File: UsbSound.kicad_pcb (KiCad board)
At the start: 4 copper layers, 121.6 x 79.8 mm, 85 parts, among them J1 SWD, J2 USB_B, J3 XLR_L, J4 XLR_R, SW1 BOOT_SELECT, U1 MP2359-LF-Z, U2 USBLC6-2SC6, U3 NE5534, U4 PCM1795DB, U5 STM32F405RGT6, U6 NE5534, U7 NE5534, U8 NE5534, Y1 16MHz, Y2 36.864MHz

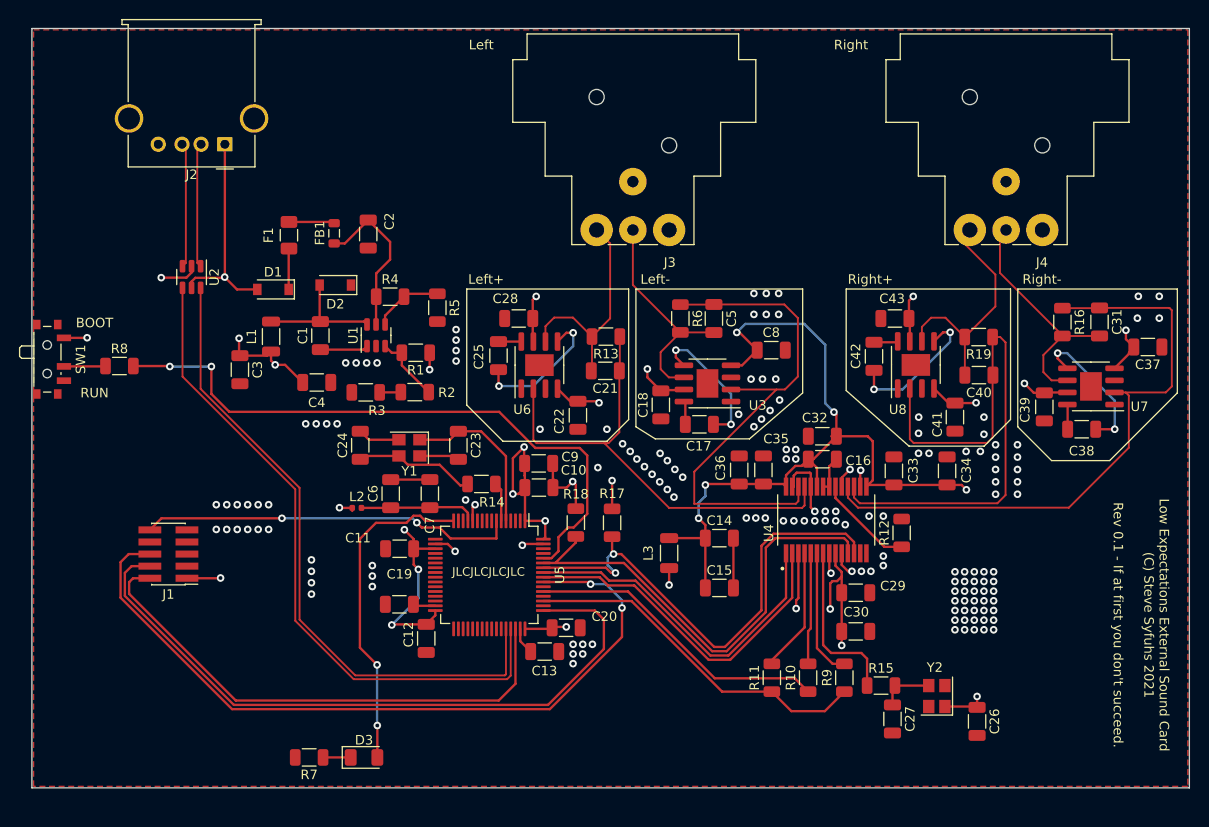
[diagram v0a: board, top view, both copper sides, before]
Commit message: Added -5v rail because I'm an idiot and forgot it
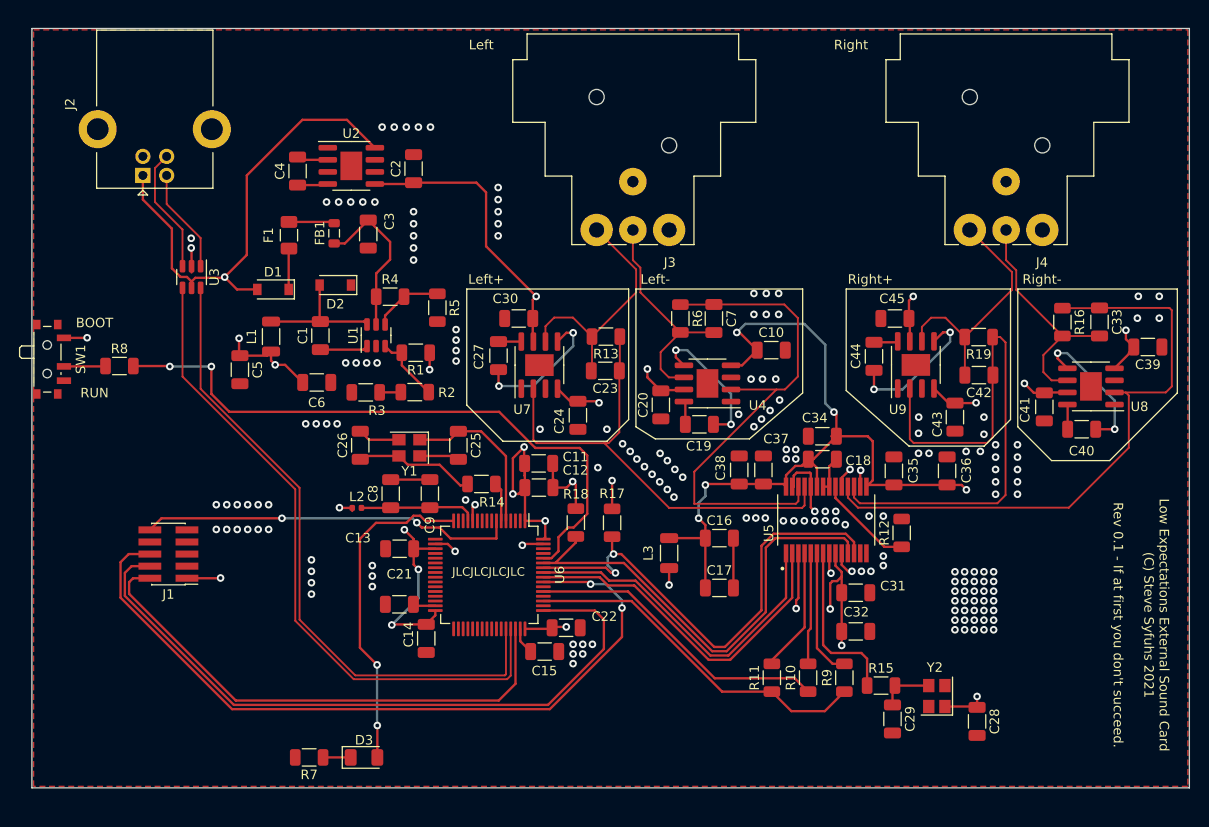
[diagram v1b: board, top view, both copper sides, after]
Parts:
- added C2: 10u, Capacitor_SMD:C_1206_3216Metric, F.Cu at (116.3, 56.2)
- added C4: 10u, Capacitor_SMD:C_1206_3216Metric, F.Cu at (104.1, 56.4)
- added U2: ICL7660, Package_SO:SOIC-8-1EP_3.9x4.9mm_P1.27mm_EP2.29x3mm, F.Cu at (109.8, 55.9)
- J2: footprint Connector_USB:USB_A_Molex_67643_Horizontal -> Connector_USB:USB_B_Lumberg_2411_02_Horizontal
- moved J2 9.22 mm to (87.9, 56.9), turned to 90 degrees
- renumbered C8 to C10, C9 to C11, C10 to C12, C11 to C13, C12 to C14, C13 to C15, C14 to C16, C15 to C17, C16 to C18, C17 to C19, C18 to C20, C19 to C21, C20 to C22, C21 to C23, C22 to C24, C23 to C25, C24 to C26, C25 to C27, C26 to C28, C27 to C29, C2 to C3, C28 to C30, C29 to C31, C30 to C32, C31 to C33, C32 to C34, C33 to C35, C34 to C36, C35 to C37, C36 to C38, C37 to C39, C38 to C40, C39 to C41, C40 to C42, C41 to C43, C42 to C44, C43 to C45, C3 to C5, C4 to C6, C5 to C7, C6 to C8, C7 to C9, U2 to U3, U3 to U4, U4 to U5, U5 to U6, U6 to U7, U7 to U8, U8 to U9
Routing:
- net +5V: track 88.0 -> 116.5 mm
- net -5VA: track 97.9 -> 123.2 mm
- net Net-(C4-Pad2): track 0.00 -> 3.30 mm
- net Net-(C4-Pad1): track 0.00 -> 3.22 mm
- net XLR_R+: track 23.9 -> 26.4 mm
- net XLR_L+: track 23.8 -> 26.1 mm
- net USB_CONN_D-: track 12.6 -> 11.0 mm
- net GND: track 54.9 -> 53.4 mm, vias 157 -> 178
- net XLR_R-: track 23.8 -> 25.0 mm
- net USB_CONN_D+: track 12.6 -> 13.3 mm

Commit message: Op Amps are better paired for line matching
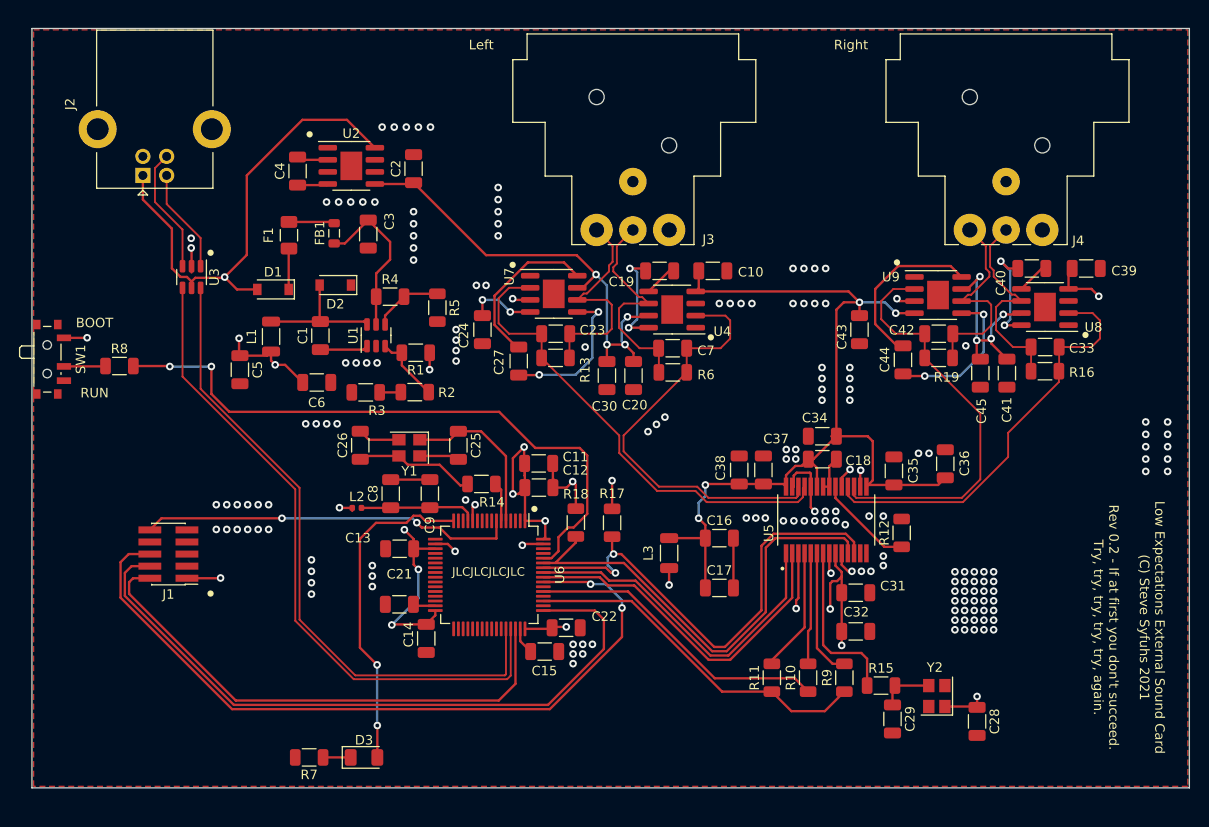
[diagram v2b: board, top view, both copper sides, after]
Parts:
- moved C40 17.7 mm to (181.3, 66.7)
- moved C19 16.7 mm to (142.2, 66.9)
- moved C43 13.6 mm to (163.2, 73.1)
- moved C24 13.5 mm to (123.6, 73.1)
- moved C30 11.0 mm to (136.7, 77.9), turned to 90 degrees
- moved C45 10.7 mm to (175.9, 77.7), turned to 90 degrees
- moved C39 10.5 mm to (187.0, 66.7)
- moved C10 10.4 mm to (147.8, 66.9)
- moved U8 9.64 mm to (182.7, 70.7)
- moved U4 8.61 mm to (143.5, 71.0)
- moved U9 7.70 mm to (171.4, 69.5), turned to 0 degrees
- moved U7 7.64 mm to (131.1, 69.3), turned to 0 degrees
- moved C23 6.51 mm to (131.3, 73.5), turned to 0 degrees
- moved C33 6.29 mm to (182.7, 74.9), turned to 180 degrees
- moved C42 6.06 mm to (171.5, 73.5), turned to 0 degrees
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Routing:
- net POUTR-: track 65.5 -> 44.0 mm
- net POUTR+: track 60.3 -> 44.0 mm
- net Net-(C44-Pad1): track 2.40 -> 18.1 mm
- net Net-(C27-Pad1): track 2.40 -> 17.3 mm
- net -5VA: track 123.2 -> 109.7 mm, vias 4 -> 8
- net Net-(C40-Pad2): track 15.1 -> 3.46 mm, vias 2 -> 0
- net Net-(C19-Pad2): track 14.7 -> 3.53 mm, vias 2 -> 0
- net POUTL-: track 54.8 -> 45.8 mm
- net Net-(C19-Pad1): track 2.24 -> 11.0 mm, vias 0 -> 2
- net Net-(C40-Pad1): track 2.57 -> 11.3 mm, vias 0 -> 2
- net +5VA: track 153.7 -> 160.3 mm, vias 8 -> 7
- net XLR_R+: track 26.4 -> 22.1 mm
- net GND: track 53.4 -> 57.3 mm, vias 178 -> 168
- net XLR_R-: track 25.0 -> 22.0 mm
- net XLR_L+: track 26.1 -> 23.3 mm
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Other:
- board text added: "Low Expectations External Sound Card (C) Steve Syfuhs 2021 Rev 0.2 - If at first you don't succeed. Try, try, try, try, try, again."
- board text removed: "Left+"
- board text removed: "Left-"
- board text removed: "Low Expectations External Sound Card (C) Steve Syfuhs 2021 Rev 0.1 - If at first you don't succeed."
- board text removed: "Right+"
- board text removed: "Right-"

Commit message: Fixing models
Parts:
- U1: value MP2359-LF-Z -> XRP7659; footprint Package_TO_SOT_SMD:SOT-23-6 -> Package_SO:TSOP-6_1.65x3.05mm_P0.95mm
- moved U1 0.13 mm to (112.5, 73.8)

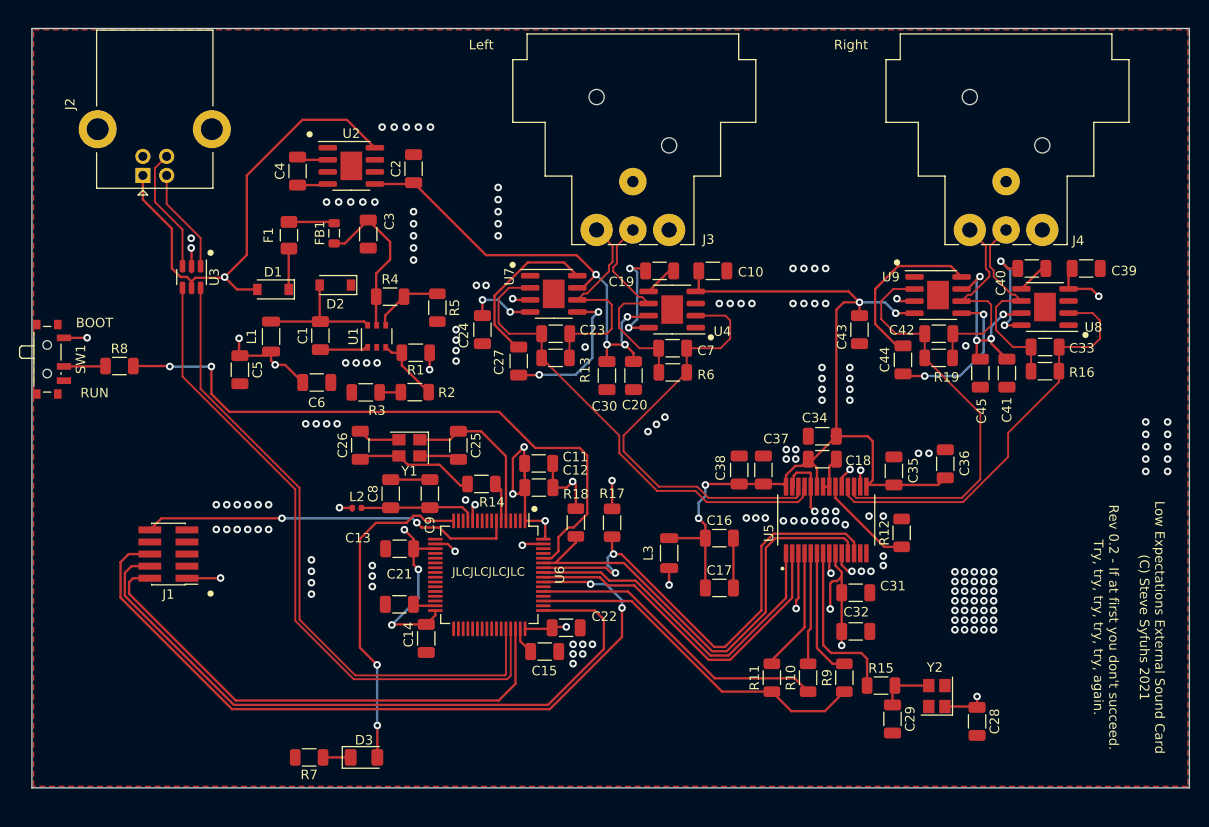
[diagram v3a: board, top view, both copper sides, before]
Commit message: More via stitching and updated image
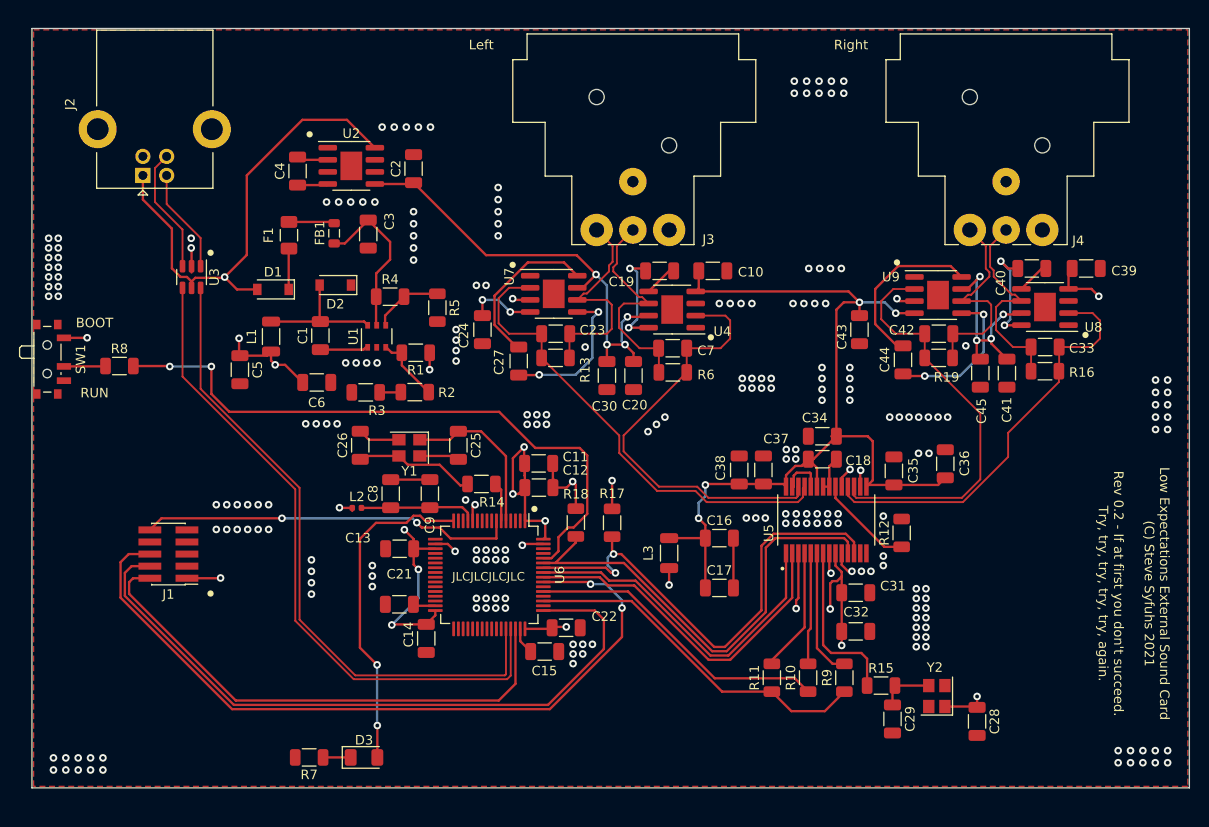
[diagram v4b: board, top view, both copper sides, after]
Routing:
- net GND: track 57.3 -> 54.5 mm, vias 168 -> 229

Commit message: Maybe fixed clock path. Moved some power routes to avoid analog signal.
Added some additional silkscreen for useful text.
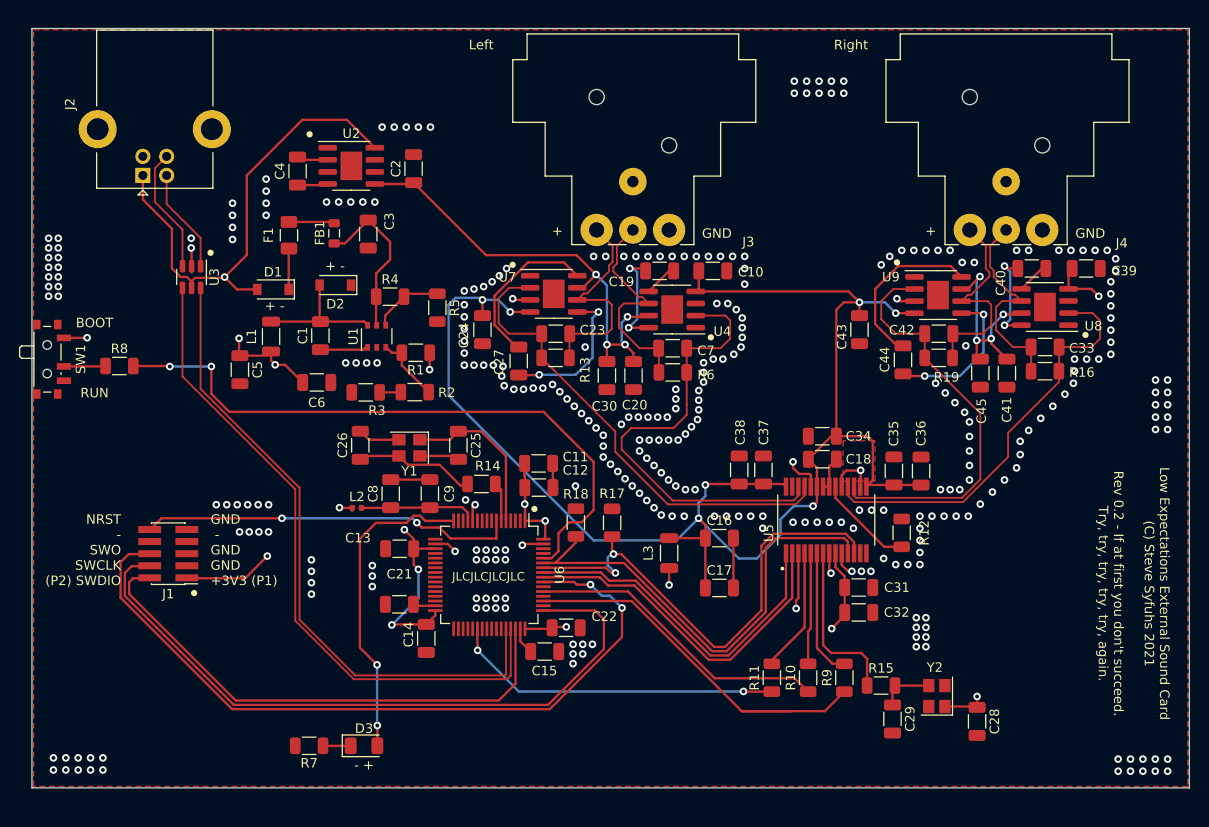
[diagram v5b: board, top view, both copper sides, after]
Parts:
- moved C36 2.65 mm to (169.7, 88.0)
- moved C32 2.01 mm to (163.1, 102.8)
- moved D3 1.22 mm to (111.1, 116.8)
- moved R7 1.22 mm to (105.4, 116.8)
- moved C31 0.63 mm to (163.1, 100.2)
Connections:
- R11 pad 1: I2S3_CK -> I2S3_MCK
- U6 pad 38: unconnected-(U6-Pad38) -> I2S3_MCK
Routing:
- net I2S3_MCK: track 0.00 -> 35.0 mm, vias 0 -> 2
- net +5VA: track 160.3 -> 190.7 mm, vias 7 -> 8
- net +3V3: track 252.3 -> 229.9 mm, vias 17 -> 15
- net GND: track 54.5 -> 46.9 mm, vias 229 -> 317
- net I2S3_CK: track 37.3 -> 42.5 mm
- net POUTL-: track 45.8 -> 48.8 mm
- net +5V: track 116.5 -> 114.7 mm
- net Net-(C40-Pad1): track 11.3 -> 10.0 mm
- net LED_STATUS: track 34.8 -> 33.6 mm
- net BOOT0: track 66.8 -> 67.8 mm
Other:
- board text added: "+"
- board text added: "+ -"
- board text added: "- +"
- board text added: "GND"
- board text added: "GND - GND GND +3V3 (P1)"
- board text added: "NRST - SWO SWCLK (P2) SWDIO"

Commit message: Added GPIO pin header for future testing
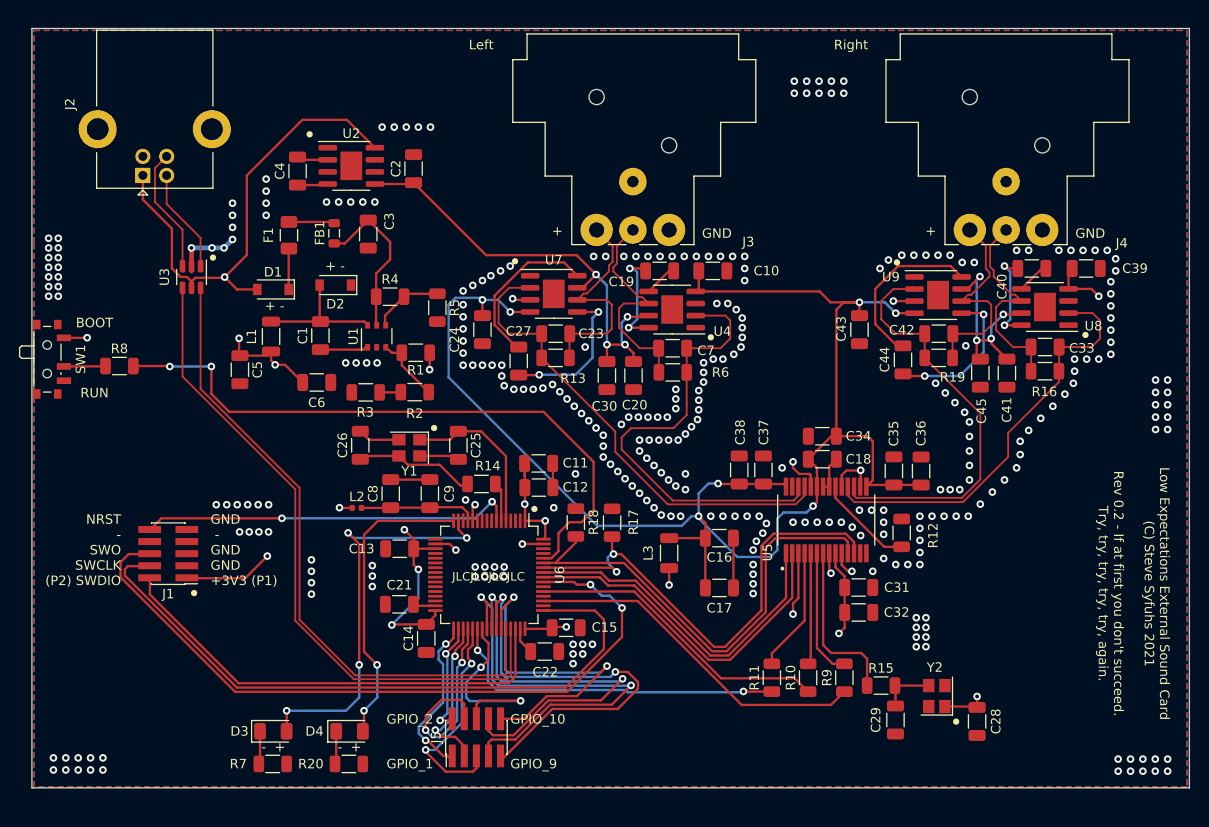
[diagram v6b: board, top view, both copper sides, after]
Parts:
- added D4: Red, LED_SMD:LED_1206_3216Metric, F.Cu at (109.6, 115.3)
- added J5: SWD, Connector_PinHeader_1.27mm:PinHeader_2x05_P1.27mm_Vertical_SMD, F.Cu at (122.9, 116.0)
- added R20: 2k2, Resistor_SMD:R_1206_3216Metric, F.Cu at (109.5, 118.7)
- moved D3 9.65 mm to (101.6, 115.3)
- moved R7 4.28 mm to (101.5, 118.7), turned to 0 degrees
- moved C29 0.33 mm to (167.0, 114.1)
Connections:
- net Net-(C18-Pad2) renamed /VCOM
- net Net-(C19-Pad1) renamed /LVAC-
- net Net-(C19-Pad2) renamed /LVA-
- net Net-(C21-Pad1) renamed /VCAP1
- net Net-(C22-Pad1) renamed /VCAP2
- net Net-(C27-Pad1) renamed /LVAC+
- net Net-(C27-Pad2) renamed /LVA+
- net Net-(C4-Pad1) renamed /CAP-
- net Net-(C4-Pad2) renamed /CAP+
- net Net-(C40-Pad1) renamed /RVAC-
- net Net-(C40-Pad2) renamed /RVA-
- net Net-(C44-Pad1) renamed /RVAC+
- net Net-(C44-Pad2) renamed /RVA+
- net Net-(R10-Pad2) renamed /I2SD
- net Net-(R11-Pad2) renamed /LRCK
- net Net-(R12-Pad1) renamed /IREF
- net Net-(R9-Pad2) renamed /BCK
- D3 pad 2: LED_STATUS -> LED_STATUS1
- U6 pad 15: unconnected-(U6-Pad15) -> LED_STATUS1
- U6 pad 16: LED_STATUS -> LED_STATUS2
- U6 pad 33: unconnected-(U6-Pad33) -> GPIO_1
- U6 pad 34: unconnected-(U6-Pad34) -> GPIO_2
- U6 pad 35: unconnected-(U6-Pad35) -> GPIO_3
- U6 pad 36: unconnected-(U6-Pad36) -> GPIO_4
- U6 pad 37: unconnected-(U6-Pad37) -> GPIO_5
- U6 pad 39: unconnected-(U6-Pad39) -> GPIO_6
- U6 pad 40: unconnected-(U6-Pad40) -> GPIO_7
- U6 pad 41: unconnected-(U6-Pad41) -> GPIO_8
- U6 pad 42: unconnected-(U6-Pad42) -> GPIO_9
- U6 pad 43: unconnected-(U6-Pad43) -> GPIO_10
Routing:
- net GPIO_7: track 0.00 -> 47.0 mm, vias 0 -> 2
- net GPIO_9: track 0.00 -> 45.1 mm, vias 0 -> 2
- net GPIO_8: track 0.00 -> 43.0 mm, vias 0 -> 2
- net LED_STATUS1: track 0.00 -> 42.9 mm, vias 0 -> 4
- net GPIO_10: track 0.00 -> 36.9 mm, vias 0 -> 2
- net LED_STATUS: track 33.6 -> 0.00 mm, vias 2 -> 0
- net LED_STATUS2: track 0.00 -> 31.9 mm, vias 0 -> 2
- net GPIO_5: track 0.00 -> 23.0 mm, vias 0 -> 2
- net GPIO_4: track 0.00 -> 23.0 mm, vias 0 -> 2
- net GPIO_6: track 0.00 -> 21.2 mm, vias 0 -> 2
- net GPIO_1: track 0.00 -> 17.7 mm, vias 0 -> 2
- net GPIO_3: track 0.00 -> 17.4 mm, vias 0 -> 2
- net GPIO_2: track 0.00 -> 12.0 mm, vias 0 -> 2
- net SWDIO: track 55.3 -> 49.3 mm
- net I2S3_CK: track 42.5 -> 36.7 mm
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- added copper zone on B.Cu, net GND
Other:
- board text added: "-"
- board text added: "GPIO_1"
- board text added: "GPIO_10"
- board text added: "GPIO_2"
- board text added: "GPIO_9"
